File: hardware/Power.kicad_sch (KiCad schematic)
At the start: 6 parts, among them U201 TPS62172DSGR

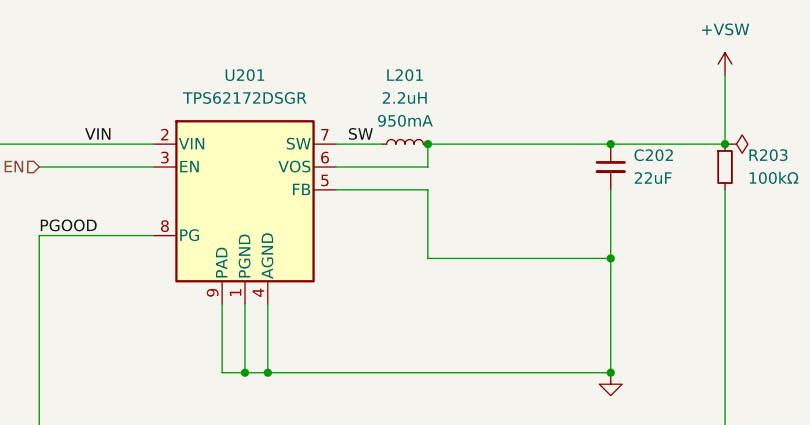
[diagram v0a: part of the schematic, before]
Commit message: Schematic and layout Progress
Signed-off-by: Connor Rigby <connorr@hey.com>
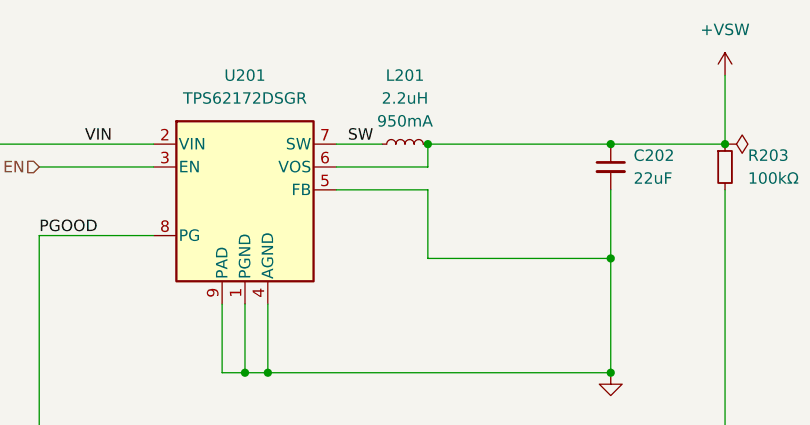
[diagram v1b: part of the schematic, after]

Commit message: Layout updates
Signed-off-by: Connor Rigby <connorr@hey.com>
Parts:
- added TP201: 3.3v, TestPoint:TestPoint_Pad_D1.0mm, symbol Connector:TestPoint
- added TP202: GND, TestPoint:TestPoint_Pad_D1.0mm, symbol Connector:TestPoint
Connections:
- net GND: now also TP202.1
- net +VSW renamed +3.3V
- net +3.3V: now also TP201.1
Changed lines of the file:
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@@
   (junction (at 106.68 50.8) (diameter 0) (color 0 0 0 0)
   )
+  (junction (at 139.7 48.26) (diameter 0) (color 0 0 0 0)
+  )
   (junction (at 127 50.8) (diameter 0) (color 0 0 0 0)
   )
@@
     (stroke (width 0) (type default))
   )
-  (wire (pts (xy 139.7 43.18) (xy 139.7 50.8))
+  (wire (pts (xy 139.7 43.18) (xy 139.7 48.26))
     (stroke (width 0) (type default))
   )
@@
   )
   (wire (pts (xy 127 63.5) (xy 127 55.88))
+    (stroke (width 0) (type default))
+  )
+  (wire (pts (xy 139.7 48.26) (xy 139.7 50.8))
     (stroke (width 0) (type default))
   )
@@
     )
   )
-  (symbol (lib_id "power:+VSW") (at 139.7 43.18 0) (unit 1)
-    (in_bom yes) (on_board yes) (dnp no) (fields_autoplaced)
-    (property "Reference" "#PWR0101" (at 139.7 46.99 0)
-      (effects (font (size 1.27 1.27)) hide)
-    )
-    (property "Value" "+VSW" (at 139.7 38.1 0)
-      (effects (font (size 1.27 1.27)))
-    )
-    (property "Footprint" "" (at 139.7 43.18 0)
-      (effects (font (size 1.27 1.27)) hide)
-    )
-    (property "Datasheet" "" (at 139.7 43.18 0)
-      (effects (font (size 1.27 1.27)) hide)
-    )
-    (pin "1")
-    (instances
-      (project "underglow2"
-        (path "/dcbdf88a-d6ac-4b1d-9514-0b0ce113d90b/51e4e0b8-920f-4548-a9c8-d97d830c9625"
-          (reference "#PWR0101") (unit 1)
-        )
-      )
-    )
-  )
   (symbol (lib_id "power:GND") (at 127 76.2 0) (unit 1)
     (in_bom yes) (on_board yes) (dnp no) (fields_autoplaced)
@@
     )
   )
+  (symbol (lib_id "Connector:TestPoint") (at 162.56 48.26 90) (unit 1)
+    (in_bom yes) (on_board yes) (dnp no)
+    (property "Reference" "TP202" (at 157.48 50.8 90)
+      (effects (font (size 1.27 1.27)) (justify left))
+    )
+    (property "Value" "GND" (at 157.48 48.26 90)
+      (effects (font (size 1.27 1.27)) (justify left))
+    )
+    (property "Footprint" "TestPoint:TestPoint_Pad_D1.0mm" (at 162.56 43.18 0)
+      (effects (font (size 1.27 1.27)) hide)
+    )
+    (property "Datasheet" "~" (at 162.56 43.18 0)
+      (effects (font (size 1.27 1.27)) hide)
+    )
+    (pin "1")
+    (instances
+      (project "underglow2"
+        (path "/dcbdf88a-d6ac-4b1d-9514-0b0ce113d90b/51e4e0b8-920f-4548-a9c8-d97d830c9625"
+          (reference "TP202") (unit 1)
+        )
+      )
+    )
+  )
   (symbol (lib_id "LCSC_Capacitor:C_0805_10u_X5R") (at 50.8 53.34 0) (unit 1)
     (in_bom yes) (on_board yes) (dnp no) (fields_autoplaced)
@@
     )
   )
+  (symbol (lib_id "power:+3.3V") (at 139.7 43.18 0) (unit 1)
+    (in_bom yes) (on_board yes) (dnp no) (fields_autoplaced)
+    (property "Reference" "#PWR0201" (at 139.7 46.99 0)
+      (effects (font (size 1.27 1.27)) hide)
+    )
+    (property "Value" "+3.3V" (at 139.7 39.37 0)
+      (effects (font (size 1.27 1.27)))
+    )
+    (property "Footprint" "" (at 139.7 43.18 0)
+      (effects (font (size 1.27 1.27)) hide)
+    )
+    (property "Datasheet" "" (at 139.7 43.18 0)
+      (effects (font (size 1.27 1.27)) hide)
+    )
+    (pin "1")
+    (instances
+      (project "underglow2"
+        (path "/dcbdf88a-d6ac-4b1d-9514-0b0ce113d90b/51e4e0b8-920f-4548-a9c8-d97d830c9625"
+          (reference "#PWR0201") (unit 1)
+        )
+      )
+    )
+  )
   (symbol (lib_id "power:GND") (at 50.8 55.88 0) (unit 1)
     (in_bom yes) (on_board yes) (dnp no) (fields_autoplaced)
@@
     )
   )
+  (symbol (lib_id "Connector:TestPoint") (at 139.7 48.26 270) (unit 1)
+    (in_bom yes) (on_board yes) (dnp no)
+    (property "Reference" "TP201" (at 144.78 45.72 90)
+      (effects (font (size 1.27 1.27)) (justify left))
+    )
+    (property "Value" "3.3v" (at 144.78 48.26 90)
+      (effects (font (size 1.27 1.27)) (justify left))
+    )
+    (property "Footprint" "TestPoint:TestPoint_Pad_D1.0mm" (at 139.7 53.34 0)
+      (effects (font (size 1.27 1.27)) hide)
+    )
+    (property "Datasheet" "~" (at 139.7 53.34 0)
+      (effects (font (size 1.27 1.27)) hide)
+    )
+    (pin "1")
+    (instances
+      (project "underglow2"
+        (path "/dcbdf88a-d6ac-4b1d-9514-0b0ce113d90b/51e4e0b8-920f-4548-a9c8-d97d830c9625"
+          (reference "TP201") (unit 1)
+        )
+      )
+    )
+  )
   (symbol (lib_id "power:PWR_FLAG") (at 139.7 50.8 270) (unit 1)
     (in_bom yes) (on_board yes) (dnp no) (fields_autoplaced)
@@
         )
       )
+    )
+  )
+  (symbol (lib_id "power:GND") (at 162.56 48.26 90) (unit 1)
+    (in_bom yes) (on_board yes) (dnp no) (fields_autoplaced)
+    (property "Reference" "#PWR0202" (at 168.91 48.26 0)
+      (effects (font (size 1.27 1.27)) hide)
+    )
+    (property "Value" "GND" (at 166.37 48.895 90)
+      (effects (font (size 1.27 1.27)) (justify right))
+    )
+    (property "Footprint" "" (at 162.56 48.26 0)
+      (effects (font (size 1.27 1.27)) hide)
+    )
+    (property "Datasheet" "" (at 162.56 48.26 0)
+      (effects (font (size 1.27 1.27)) hide)
+    )
+    (pin "1")
+    (instances
+      (project "underglow2"
+        (path "/dcbdf88a-d6ac-4b1d-9514-0b0ce113d90b/51e4e0b8-920f-4548-a9c8-d97d830c9625"
+          (reference "#PWR0202") (unit 1)
+        )
+      )

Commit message: Almost ready for fab
Signed-off-by: Connor Rigby <connorr@hey.com>
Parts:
- added D201: LED_0603_RED, LED_SMD:LED_0603_1608Metric, symbol LCSC_LED:LED_0603_RED
- added R201: R_0603_330, Resistor_SMD:R_0603_1608Metric, symbol LCSC_Resistor:R_0603_330
- TP201, TP202: now left out of the parts list
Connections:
- net +3.3V: now also R201.1
- net GND: now also D201.1 (K)
- new net: D201.2 (A), R201.2
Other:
- moved on the sheet: C202, R203, TP202

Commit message: Pre-production updates
Signed-off-by: Connor Rigby <connorr@hey.com>
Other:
- company: (none) -> https://cone.codes
- title: (none) -> coneRGB2
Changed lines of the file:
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@@
   (paper "A5")
   (title_block
-    (date "2023-02-28")
+    (title "coneRGB2")
+    (date "2023-03-20")
+    (rev "1")
+    (company "https://cone.codes")
+    (comment 1 "https://github.com/connorrigby/underglow2")
+    (comment 2 "Designed by Connor Rigby")
+    (comment 3 "Buck regulator taking ~8-20v and steps down to 3.3v")
+    (comment 4 "Voltage Regulator")
   )
   (junction (at 127 63.5) (diameter 0) (color 0 0 0 0)
@@
     (stroke (width 0) (type default))
   )
+  (text_box "PGOOD can be used as a fault indicator or similar functionality\nTODO: add an LED"
+    (at 15.24 60.96 0) (size 43.18 7.62)
+    (stroke (width 0) (type default))
+    (fill (type none))
+    (effects (font (size 1.27 1.27)) (justify left top))
+  )
   (label "SW" (at 97.79 50.8 0) (fields_autoplaced)

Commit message: hardware: add USB for debugging and programming
Signed-off-by: Connor Rigby <connorr@hey.com>
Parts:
- added D202, D203: D_Small, Diode_SMD:D_SMA, symbol Device:D_Small
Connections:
- net +12V: now also D202.2 (A); no longer F201.1
- new net: D202.1 (K), D203.1 (K), F201.1
- new net +5V: D203.2 (A)
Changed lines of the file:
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@@
   (junction (at 127 63.5) (diameter 0) (color 0 0 0 0)
   )
+  (junction (at 35.56 50.8) (diameter 0) (color 0 0 0 0)
+  )
   (junction (at 106.68 50.8) (diameter 0) (color 0 0 0 0)
   )
@@
   (junction (at 139.7 43.18) (diameter 0) (color 0 0 0 0)
   )
+  (wire (pts (xy 33.02 58.42) (xy 35.56 58.42))
+    (stroke (width 0) (type default))
+  )
   (wire (pts (xy 127 76.2) (xy 88.9 76.2))
     (stroke (width 0) (type default))
@@
     (stroke (width 0) (type default))
   )
+  (wire (pts (xy 35.56 58.42) (xy 35.56 50.8))
+    (stroke (width 0) (type default))
+  )
   (wire (pts (xy 106.68 55.88) (xy 106.68 63.5))
     (stroke (width 0) (type default))
   )
+  (wire (pts (xy 15.24 58.42) (xy 27.94 58.42))
+    (stroke (width 0) (type default))
+  )
   (wire (pts (xy 96.52 53.34) (xy 106.68 53.34))
     (stroke (width 0) (type default))
@@
     (stroke (width 0) (type default))
   )
+  (wire (pts (xy 35.56 50.8) (xy 38.1 50.8))
+    (stroke (width 0) (type default))
+  )
   (wire (pts (xy 86.36 68.58) (xy 86.36 76.2))
     (stroke (width 0) (type default))
   )
-  (wire (pts (xy 25.4 50.8) (xy 38.1 50.8))
+  (wire (pts (xy 15.24 50.8) (xy 27.94 50.8))
     (stroke (width 0) (type default))
   )
@@
   )
   (wire (pts (xy 139.7 48.26) (xy 139.7 50.8))
+    (stroke (width 0) (type default))
+  )
+  (wire (pts (xy 33.02 50.8) (xy 35.56 50.8))
     (stroke (width 0) (type default))
   )
@@
     )
   )
+  (symbol (lib_id "Device:D_Small") (at 30.48 58.42 180) (unit 1)
+    (in_bom yes) (on_board yes) (dnp no) (fields_autoplaced)
+    (property "Reference" "D203" (at 30.48 55.88 0)
+      (effects (font (size 1.27 1.27)))
+    )
+    (property "Value" "D_Small" (at 30.48 55.88 0)
+      (effects (font (size 1.27 1.27)) hide)
+    )
+    (property "Footprint" "Diode_SMD:D_SMA" (at 30.48 58.42 90)
+      (effects (font (size 1.27 1.27)) hide)
+    )
+    (property "Datasheet" "~" (at 30.48 58.42 90)
+      (effects (font (size 1.27 1.27)) hide)
+    )
+    (property "Sim.Device" "D" (at 30.48 58.42 0)
+      (effects (font (size 1.27 1.27)) hide)
+    )
+    (property "Sim.Pins" "1=K 2=A" (at 30.48 58.42 0)
+      (effects (font (size 1.27 1.27)) hide)
+    )
+    (pin "1")
+    (pin "2")
+    (instances
+      (project "underglow2"
+        (path "/dcbdf88a-d6ac-4b1d-9514-0b0ce113d90b/51e4e0b8-920f-4548-a9c8-d97d830c9625"
+          (reference "D203") (unit 1)
+        )
+      )
+    )
+  )
   (symbol (lib_id "LCSC_LED:LED_0603_RED") (at 152.4 66.04 90) (unit 1)
     (in_bom yes) (on_board yes) (dnp no) (fields_autoplaced)
@@
     )
   )
+  (symbol (lib_id "power:+5V") (at 15.24 58.42 0) (unit 1)
+    (in_bom yes) (on_board yes) (dnp no) (fields_autoplaced)
+    (property "Reference" "#PWR0203" (at 15.24 62.23 0)
+      (effects (font (size 1.27 1.27)) hide)
+    )
+    (property "Value" "+5V" (at 15.24 54.61 0)
+      (effects (font (size 1.27 1.27)))
+    )
+    (property "Footprint" "" (at 15.24 58.42 0)
+      (effects (font (size 1.27 1.27)) hide)
+    )
+    (property "Datasheet" "" (at 15.24 58.42 0)
+      (effects (font (size 1.27 1.27)) hide)
+    )
+    (pin "1")
+    (instances
+      (project "underglow2"
+        (path "/dcbdf88a-d6ac-4b1d-9514-0b0ce113d90b/51e4e0b8-920f-4548-a9c8-d97d830c9625"
+          (reference "#PWR0203") (unit 1)
+        )
+      )
+    )
+  )
   (symbol (lib_id "LCSC_Capacitor:C_0805_10u_X5R") (at 50.8 53.34 0) (unit 1)
     (in_bom yes) (on_board yes) (dnp no) (fields_autoplaced)
@@
     )
   )
-  (symbol (lib_id "power:+12V") (at 25.4 50.8 0) (unit 1)
-    (in_bom yes) (on_board yes) (dnp no) (fields_autoplaced)
-    (property "Reference" "#PWR0103" (at 25.4 54.61 0)
-      (effects (font (size 1.27 1.27)) hide)
-    )
-    (property "Value" "+12V" (at 25.4 45.72 0)
-      (effects (font (size 1.27 1.27)))
-    )
-    (property "Footprint" "" (at 25.4 50.8 0)
-      (effects (font (size 1.27 1.27)) hide)
-    )
-    (property "Datasheet" "" (at 25.4 50.8 0)
-      (effects (font (size 1.27 1.27)) hide)
-    )
+  (symbol (lib_id "Device:D_Small") (at 30.48 50.8 180) (unit 1)
+    (in_bom yes) (on_board yes) (dnp no) (fields_autoplaced)
+    (property "Reference" "D202" (at 30.48 48.26 0)
+      (effects (font (size 1.27 1.27)))
+    )
+    (property "Value" "D_Small" (at 30.48 48.26 0)
+      (effects (font (size 1.27 1.27)) hide)
+    )
+    (property "Footprint" "Diode_SMD:D_SMA" (at 30.48 50.8 90)
+      (effects (font (size 1.27 1.27)) hide)
+    )
+    (property "Datasheet" "~" (at 30.48 50.8 90)
+      (effects (font (size 1.27 1.27)) hide)
+    )
+    (property "Sim.Device" "D" (at 30.48 50.8 0)
+      (effects (font (size 1.27 1.27)) hide)
+    )
+    (property "Sim.Pins" "1=K 2=A" (at 30.48 50.8 0)
+      (effects (font (size 1.27 1.27)) hide)
+    )
+    (pin "1")
+    (pin "2")
+    (instances
+      (project "underglow2"
+        (path "/dcbdf88a-d6ac-4b1d-9514-0b0ce113d90b/51e4e0b8-920f-4548-a9c8-d97d830c9625"
+          (reference "D202") (unit 1)
+        )
+      )
+    )
+  )
+  (symbol (lib_id "power:+12V") (at 15.24 50.8 0) (unit 1)
+    (in_bom yes) (on_board yes) (dnp no) (fields_autoplaced)
+    (property "Reference" "#PWR0103" (at 15.24 54.61 0)
+      (effects (font (size 1.27 1.27)) hide)
+    )
+    (property "Value" "+12V" (at 15.24 45.72 0)
+      (effects (font (size 1.27 1.27)))
+    )
+    (property "Footprint" "" (at 15.24 50.8 0)
+      (effects (font (size 1.27 1.27)) hide)
+    )
+    (property "Datasheet" "" (at 15.24 50.8 0)
+      (effects (font (size 1.27 1.27)) hide)
+    )

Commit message: Rev 2 submitted for production
Signed-off-by: Connor Rigby <connorr@hey.com>
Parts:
- removed C202: C_0805_22u_X7R, Capacitor_SMD:C_0805_2012Metric, symbol LCSC_Capacitor:C_0805_22u_X7R
- removed D202, D203: D_Small, Diode_SMD:D_SMA, symbol Device:D_Small
- removed L201: L_0805_2u2, Inductor_SMD:L_0805_2012Metric, symbol LCSC_Power_Inductor:L_0805_2u2
- removed R201: R_0603_330, Resistor_SMD:R_0603_1608Metric, symbol LCSC_Resistor:R_0603_330
- removed R203: R_0603_100k, Resistor_SMD:R_0603_1608Metric, symbol LCSC_Resistor:R_0603_100k
- removed U201: TPS62172DSGR, Package_SON:WSON-8-1EP_2x2mm_P0.5mm_EP0.9x1.6mm_ThermalVias, symbol LCSC_Regulator:TPS62172DSGR
- added C202: C_0805_1u_X7R, Capacitor_SMD:C_0805_2012Metric, symbol LCSC_Capacitor:C_0805_1u_X7R
- added D202: 30v 230mv@100ma 1A, Diode_SMD:D_SOD-323F, symbol Device:D_Schottky
- added Q301: AO4803A, Package_SO:SOP-8_3.76x4.96mm_P1.27mm, symbol LCSC_MOSFET:AO4803A
- added R201: R_0603_499, Resistor_SMD:R_0603_1608Metric, symbol LCSC_Resistor:R_0603_499
- added R203, R206: R_0805_10k, Resistor_SMD:R_0805_2012Metric, symbol LCSC_Resistor:R_0805_10k
- added R204, R205: R_0603_DNP, Resistor_SMD:R_0603_1608Metric, symbol LCSC_Resistor:R_0603_DNP
- added R207: R_0805_4k7, Resistor_SMD:R_0805_2012Metric, symbol LCSC_Resistor:R_0805_4k7
- added U201: SPX3819M5-L-3-3_TR, Package_TO_SOT_SMD:SOT-23-5, symbol LCSC_DCDC_Converter:SPX3819M5-L-3-3_TR
- added U301: MCP1416, Package_TO_SOT_SMD:SOT-23-5, symbol LCSC_MOSFET:MCP1416
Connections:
- net +12V: now also D202.2 (A)
- net EN: now also R206.2, U301.3 (IN)
- net GND: now also C202.2, R203.2, R205.2, R206.1, U201.2 (GND), U301.4 (GND)
- net VIN: now also U201.1 (IN)
- net at F201.1: now also Q301.3 (S), Q301.7 (D), Q301.8 (G)
- net at D201.2 (A): now also R201.2
- net +3.3V renamed VDD
- net VDD: now also C202.1, R201.1, R204.1, U201.5 (OUT)
- new net: Q301.5 (D), Q301.6 (G), U201.3 (EN)
- new net BYP: R204.2, R205.1, U201.4 (BYP)
- new net VIN_DIODE: D202.1 (K), R207.1
- new net VIN_DIV: Q301.1 (S), R203.1, R207.2, U301.2 (Vdd)
- new net VIN_GATE: Q301.2 (G), Q301.4 (G), U301.5 (OUT)
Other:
- moved on the sheet: C201, D201, F201, TP201, TP202

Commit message: ughhhhhhhhhhhhhhhhhhhhhhhhhhhhhhhhhhhhhhhhhhhhhhhhhhh
Signed-off-by: Connor Rigby <connorr@hey.com>
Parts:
- removed C201: C_0805_10u_X5R, Capacitor_SMD:C_0805_2012Metric, symbol LCSC_Capacitor:C_0805_10u_X5R
- removed C202: C_0805_1u_X7R, Capacitor_SMD:C_0805_2012Metric, symbol LCSC_Capacitor:C_0805_1u_X7R
- removed F201: nSMD010, Fuse:Fuse_1206_3216Metric, symbol LCSC_Fuse:nSMD010
- removed Q301: AO4803A, Package_SO:SOP-8_3.76x4.96mm_P1.27mm, symbol LCSC_MOSFET:AO4803A
- removed R201: R_0603_499, Resistor_SMD:R_0603_1608Metric, symbol LCSC_Resistor:R_0603_499
- removed R204, R205: R_0603_DNP, Resistor_SMD:R_0603_1608Metric, symbol LCSC_Resistor:R_0603_DNP
- removed R206: R_0805_10k, Resistor_SMD:R_0805_2012Metric, symbol LCSC_Resistor:R_0805_10k
- removed TP201: 3.3v, TestPoint:TestPoint_Pad_D1.0mm, symbol Connector:TestPoint
- removed TP202: GND, TestPoint:TestPoint_Pad_D1.0mm, symbol Connector:TestPoint
- removed U201: SPX3819M5-L-3-3_TR, Package_TO_SOT_SMD:SOT-23-5, symbol LCSC_DCDC_Converter:SPX3819M5-L-3-3_TR
- removed U301: MCP1416, Package_TO_SOT_SMD:SOT-23-5, symbol LCSC_MOSFET:MCP1416
- added BT201: Backup, Battery:BatteryHolder_Seiko_MS621F, symbol Device:Battery_Cell
- added C201, C205: C_0805_22u_X7R, Capacitor_SMD:C_0805_2012Metric, symbol LCSC_Capacitor:C_0805_22u_X7R
- added C202, C203: C_0805_10u_X5R, Capacitor_SMD:C_0805_2012Metric, symbol LCSC_Capacitor:C_0805_10u_X5R
- added C204: C_0805_1u_X7R, Capacitor_SMD:C_0805_2012Metric, symbol LCSC_Capacitor:C_0805_1u_X7R
- added D203: LED_0603_RED, LED_SMD:LED_0603_1608Metric, symbol LCSC_LED:LED_0603_RED
- added D204: BAT54C, Package_TO_SOT_SMD:SOT-23, symbol Diode:BAT54C
- added R201, R202: R_0603_2k, Resistor_SMD:R_0603_1608Metric, symbol LCSC_Resistor:R_0603_2k
- added U201: AMS1117-5.0, Package_TO_SOT_SMD:SOT-223-3_TabPin2, symbol Regulator_Linear:AMS1117-5.0
- added U202: AMS1117-3.3, Package_TO_SOT_SMD:SOT-223-3_TabPin2, symbol Regulator_Linear:AMS1117-3.3
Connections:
- net GND: now also BT201.2 (-), C201.2, C202.2, C203.2, C204.2, C205.2, R201.2, R202.2, U201.1 (GND), U202.1 (GND); no longer D201.1 (K)
- net VDD: now also C203.1, D203.2 (A), D204.2, U202.2 (VO)
- net VIN_DIV: now also C201.1, U201.3 (VI)
- net +5V: now reaches D201.2 (A)
- net +5V: now also C202.1, C204.1, U201.2 (VO), U202.3 (VI)
- new net: D201.1 (K), R201.1
- new net: BT201.1 (+), C205.1, D204.1
- new net: D203.1 (K), R202.1
- new net +BATT: D204.3

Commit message: asdf
Signed-off-by: Connor Rigby <connorr@hey.com>
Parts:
- removed R203: R_0805_10k, Resistor_SMD:R_0805_2012Metric, symbol LCSC_Resistor:R_0805_10k
- removed R207: R_0805_4k7, Resistor_SMD:R_0805_2012Metric, symbol LCSC_Resistor:R_0805_4k7
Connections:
- net VIN_DIV is gone; now on net VIN: C201.1, U201.3 (VI)
- net VIN_DIODE renamed VIN
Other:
- moved on the sheet: C201, C205, D204
